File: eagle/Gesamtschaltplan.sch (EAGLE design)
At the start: 26 parts, among them IC3 7818TV, X1 MKDSN1,5/2-5,08, X2 MKDSN1,5/2-5,08, X3 MKDSN1,5/2-5,08

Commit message: Added 'Gesamtschaltplan'
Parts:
- added 1: SUMMER4, 0liver:SUMMER4
- added C10, C11: 22pF, resistor:C-EUC0603K
- added C12, C14: 100 nF, resistor:C-EUC0603
- added C13, C3: 1µ, rcl:CPOL-EUE5-8.5
- added C15, C16, C9: 100 µF, rcl:CPOL-EUE2.5-7
- added C17, C19, C22, C23, C25, C26: 100nF, rcl:C-EUC0805
- added C18, C20, C21: 1000µ, rcl:CPOL-EUE5-13
- added C24: 1000µ, rcl:CPOL-EUE3.5-8
- added C27: 47000 uF, rcl:CPOL-EUE5-9VAXIAL
- added C28, C29: 100000uF, rcl:CPOL-EUE5-9VAXIAL
- added D10, D11, D12, D13, D5, D6, D7, D8, D9: 1N4004, diode:1N4004
- added D14, D15, D16: 38V, diode:ZENER-DIODEC1702-15
- added D4: (no value), diode:ZENER-DIODESOT23
- added DIS1: EA_DIP, display-lcd:EA_DIP
- added F1, F2: (no value), fuse:GSH15
- added IC4: 7818TV, linear:7805TV
- added IC5: DCDC-WANDLER, 0liver:DCDC-WANDLER
- added JP10, JP11, JP13, JP14, JP15, JP16, JP18, JP6: (no value), pinhead:PINHD-1X2
- added JP12: (no value), pinhead:PINHD-1X5
- added JP7: (no value), pinhead:PINHD-1X16
- added JP8: (no value), pinhead:PINHD-2X3
- added JP9: (no value), pinhead:PINHD-1X4
- added LED1, LED2: (no value), led:LED5MM
- added Q1: BC550C, transistor-npn:BC550C
- added Q10, Q11, Q12, Q13, Q14, Q15, Q16, Q17, Q18, Q19, Q20, Q21, Q8, Q9: AUIRF8409, transistor-power:PMOSFET_NTO220BH
- added Q2, Q3, Q4, Q5, Q6, Q7: IRF1234, transistor-power:PMOSFET_NTO220BH
- added R10, R12, R13, R14: 150, resistor:R-EU_0411/15
- added R11: 10k, pot:TRIM_EU-PT10
- added R15, R6, R8: 560, resistor:R-EU_R1206
- added R16, R7, R9: 3k9, resistor:R-EU_R1206
- added R17: 180R, rcl:R-EU_R1206
- added R18, R29, R30, R49: (no value), pot:TRIM_EU-PT10
- added R19, R23, R24, R25, R26, R27, R31, R32, R33, R34, R35, R36, R37: 10R, rcl:R-EU_R1206
- added R22, R38, R47: 50k, rcl:R-EU_R1206
- added R28, R39, R48: 22k 1W, rcl:R-EU_R1206
- added R3: 33k, resistor:R-EU_R1206
- added R4: 220, resistor:R-EU_R1206
- added R40, R41, R42, R43, R44, R45, R46: 10, rcl:R-EU_R1206
- added R5: 150R, rcl:R-EU_R1206
- added R50, R51, R52, R53, R54, R55, R56, R57, R58, R59: 20R 1W, rcl:R-EU_R1206
- added R60: 5R6 50W, rcl:R-EU_R1206
- added R61: 2k, rcl:R-EU_R1206
- added S1: PVA1F, switch-misc:PVA1F
- added S2, S3, S4: 9450-1, switch-misc:9450-1
- added S5: (no value), switch:255SB
- added TR1, TR2: (no value), trafo:EI38-1
- added U$1, U$6: GLEICHRICHTER, Gleichrichter:GLEICHRICHTER
- added U$3, U$4, U$5: MCP1407MCP1407-DIL08, 0liver:MCP1407MCP1407-DIL08
- added U$7: VOLTMETER, 0liver:VOLTMETER
- added X4, X5, X6: MKDSN1,5/2-5,08, con-phoenix-508:MKDSN1,5/2-5,08
- added X7: 1751251, con-phoenix-350:1751251
- C1, C7: value 100nF -> 1n; device rcl:C-EUC0805 -> rcl:C-EUC0603K
- C2: value 1000µ -> 1n; device rcl:CPOL-EUE5-13 -> rcl:C-EUC0603K
- C4: value 1000µ -> 100 nF; device rcl:CPOL-EUE5-13 -> resistor:C-EUC0603
- C5: value 100nF -> 1µ; device rcl:C-EUC0805 -> rcl:CPOL-EUE5-8.5
- C6: value 100nF -> 100 nF; device rcl:C-EUC0805 -> resistor:C-EUC0603
- C8: value 1000µ -> 100 µF; device rcl:CPOL-EUE5-13 -> rcl:CPOL-EUE2.5-7
- D1, D2: value 1N4004 -> (none); device diode:1N4004 -> diode:ZENER-DIODESOT23
- IC1, IC2: value (none) -> LM350T
- IC3: value 7818TV -> ATMEGA328P; device linear:7805TV -> avr-6:MEGA48/88/168-PU
- JP5: device pinhead:PINHD-1X2 -> pinhead:PINHD-1X4
- R1: value 180 -> 150R
- R2: value (none) -> 1k; device pot:TRIM_EU-PT10 -> resistor:R-EU_R1206
- R20: value 180 -> 180R
- U$2: value GLEICHRICHTER -> ABRACON_ABM3_CRYSTALABM03_HC49; device Gleichrichter:GLEICHRICHTER -> Ava:ABRACON_ABM3_CRYSTALABM03_HC49
- X1: value MKDSN1,5/2-5,08 -> MKDSN1,5/3-5,08; device con-phoenix-508:MKDSN1,5/2-5,08 -> con-phoenix-508:MKDSN1,5/3-5,08
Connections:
- removed net N$17: C1.1, C2.+, C4.+, C5.1, C7.1, C8.+, D1.C, D2.C, D3.C, IC1.IN, IC2.IN, IC3.VI, U$2.+
- new net C1V: D7.A, D9.A, JP1.1, JP5.3, R50.1, R51.1, R52.1, R53.1, R54.1, R9.1, U$7.P$1
- new net C1V1: R55.1, R56.1, R57.1, R58.1, R59.1
- new net C2V: C27.+, D12.A, D15.C, D8.C, JP5.1, Q2.D, Q3.D, Q4.D, Q5.D, Q6.D, Q7.D, R28.2, R7.1
- new net DATA0: DIS1.D4, IC3.PD2(INT0/PCINT18), JP7.11
- new net DATA1: DIS1.D5, IC3.PD3(INT1/OC2B/PCINT19), JP7.12
- new net DATA2: DIS1.D6, IC3.PD4(T0/XCK/PCINT20), JP7.13
- new net DATA3: DIS1.D7, IC3.PD5(T1/OC0B/PCINT21), JP7.14
- new net FET1: JP12.5, U$5.IN
- new net FET2: IC3.PD6(AIN0/OC0A/PCINT22), JP12.4, JP9.2, U$4.IN
- new net FET3: IC3.PD7(AIN1/PCINT23), JP12.3, JP9.3, U$3.IN
- new net GND1: C5.-, C6.2, U$4.GND
- new net LED: IC3.PB0(ICP1/CLKO/PCINT0), R4.1
- new net MISO: IC3.PB4(MISO/PCINT4), JP8.1, JP9.1
- new net MOSI: IC3.PB3(MOSI/OC2A/PCINT3), JP8.4
- new net N$1: JP11.1, LED2.A, R5.1
- new net N$10: IC3.PC0(ADC0/PCINT8), JP2.2, S5.S
- new net N$11: LED1.C
- new net N$12: IC3.PC1(ADC1/PCINT9), JP3.2, S4.S
- new net N$13: 1.-, JP4.2, R49.E
- new net N$14: D13.A, R61.2
- new net N$16: C15.-, C16.-, C8.-, C9.-, R10.2, R12.2, R13.2, R14.2
- new net N$18: C2.2, D2.A, IC3.PC2(ADC2/PCINT10), R15.1, R16.2
- new net N$19: S3.S
- new net N$20: IC1.ADJ, JP13.1, R20.1, R29.A
- new net N$21: D8.A
- new net N$22: JP4.1, Q1.E, R49.A, R49.S
- new net N$23: JP14.2, R18.A, R30.E, R30.S
- new net N$26: IC3.PB1(OC1A/PCINT1), R1.2
- new net N$27: C11.1, IC3.PB7(XTAL2/TOSC2/PCINT7), U$2.2
- new net N$35: D12.C, S2.O
- new net N$36: C17.1, C18.+, C19.1, C20.+, C21.+, C22.1, D3.C, D5.C, D6.C, IC1.IN, IC2.IN, IC4.VI, U$1.+
- new net N$37: C23.1, D6.A, IC4.VO, JP16.1
- new net N$38: C24.+, C25.1, IC5.VI, U$6.+
- new net N$39: S12.S, TR1.P1, TR2.P2, X5-1.KL
- new net N$40: F2.2, TR1.P2, X5-2.KL
- new net N$41: TR1.S3, U$6.AC2
- new net N$42: TR1.S4, U$6.AC1
- new net N$43: Q5.G, R19.2
- new net N$44: Q2.G, R23.2
- new net N$45: Q3.G, R24.2
- new net N$46: S12.P, X7-2.K
- new net N$47: DIS1.A, JP7.15, R4.2
- new net N$48: TR2.S4
- new net N$49: S11.P, X7-3.K
- new net N$50: F1.1, F2.1, S11.S
- new net N$51: F1.2, TR2.P1
- new net N$52: Q4.G, R25.2
- new net N$53: Q6.G, R26.2
- new net N$54: Q7.G, R27.2
- new net N$55: R19.1, R22.1, R23.1, R24.1, R25.1, R26.1, R27.1, U$5.OUT, X1-1.KL
- new net N$56: R55.2, R56.2, R57.2, R58.2, R59.2
- new net N$57: D3.A, IC1.OUT, R20.2, R50.2, R51.2, R52.2, R53.2, R54.2, X3-2.KL
- new net N$59: IC2.ADJ, JP14.1, R17.1
- new net N$6: JP6.1, LED1.A, R1.1
- new net N$60: D5.A, IC2.OUT, R17.2, X4-2.KL
- new net N$61: Q8.G, R31.2
- new net N$62: Q9.G, R32.2
- new net N$63: Q10.G, R33.2
- new net N$64: Q11.G, R34.2
- new net N$65: Q12.G, R35.2
- new net N$66: Q13.G, R36.2
- new net N$67: Q14.G, R37.2
- new net N$68: R31.1, R32.1, R33.1, R34.1, R35.1, R36.1, R37.1, R38.1, U$4.OUT, X1-2.KL
- new net N$69: C29.+, D10.A, D14.C, D9.C, Q10.D, Q11.D, Q12.D, Q13.D, Q14.D, Q8.D, Q9.D, R39.2
- new net N$7: C1.2, D1.A, IC3.PC3(ADC3/PCINT11), R6.1, R7.2
- new net N$70: Q15.G, R40.2
- new net N$71: Q16.G, R41.2
- new net N$72: Q17.G, R42.2
- new net N$73: Q18.G, R43.2
- new net N$74: Q19.G, R44.2
- new net N$75: Q20.G, R45.2
- new net N$76: Q21.G, R46.2
- new net N$77: R40.1, R41.1, R42.1, R43.1, R44.1, R45.1, R46.1, R47.1, U$3.OUT, X1-3.KL
- new net N$78: C28.+, D11.A, D16.C, D7.C, Q15.D, Q16.D, Q17.D, Q18.D, Q19.D, Q20.D, Q21.D, R48.2
- new net N$8: DIS1.VEE, JP7.3, R11.S
- new net N$9: IC3.PB2(SS/OC1B/PCINT2), R2.1, R3.1
- new net PE: X7-1.K
- new net RES: IC3.PC6(/RESET/PCINT14), JP8.5
- new net RS: DIS1.RS, IC3.PD0(RXD/PCINT16), JP7.4
- new net RW: DIS1.E, IC3.PD1(TXD/PCINT17), JP7.6
- new net SCK: IC3.PB5(SCK/PCINT5), JP8.3
- new net SENV: D13.C, JP5.4, Q10.S, Q11.S, Q12.S, Q13.S, Q14.S, Q15.S, Q16.S, Q17.S, Q18.S, Q19.S, Q2.S, Q20.S, Q21.S, Q3.S, Q4.S, Q5.S, Q6.S, Q7.S, Q8.S, Q9.S, R16.1, X6-2.KL
- new net VCC: C12.1, C26.1, DIS1.VDD, IC3.AREF, IC3.AVCC, IC3.VCC@1, IC5.VO, JP10.2, JP18.1, JP7.2, JP8.2, Q1.C, R11.A
- net GND: now also 1.+, C1.1, C10.2, C11.2, C12.2, C13.-, C14.2, C17.2, C18.-, C19.2, C2.1, C20.-, C21.-, C22.2, C23.2, C24.-, C25.2, C26.2, C27.-, C28.-, C29.-, C3.-, C4.2, C7.1, D1.C, D14.A, D15.A, D16.A, D2.C, D4.C, DIS1.C, DIS1.R/W, DIS1.VSS, IC3.AGND, IC3.GND@1, IC4.GND, IC5.GND, JP1.2, JP10.1, JP11.2, JP12.1, JP15.1, JP15.2, JP16.2, JP18.2, JP2.1, JP6.2, JP7.1, JP7.16, JP7.5, JP8.6, JP9.4, LED2.C, R10.1, R11.E, R12.1, R13.1, R14.1, R15.2, R18.E, R18.S, R22.2, R28.1, R3.2, R38.2, R39.1, R47.2, R48.1, R6.2, R60.2, R8.2, S5.P, U$1.-, U$3.GND, U$5.GND, U$6.-, U$7.P$2, X4-1.KL, X6-1.KL; no longer C1.2, C2.-, C4.-, C5.2, C6.2, C7.2, C8.-, IC3.GND, JP3.2, JP4.2, R2.E, R2.S, U$2.-, X2-1.KL
- net N$2: now also IC3.PC5(ADC5/SCLPCINT13), R5.2; no longer C6.1, D2.A, IC3.VO, JP4.1, JP5.1
- net N$24: now also U$1.AC1, X2-2.KL; no longer U$2.AC1, X1-2.KL
- net N$25: now also TR2.S3, U$1.AC2, X2-1.KL; no longer U$2.AC2, X1-1.KL
- net N$28: now also C10.1, IC3.PB6(XTAL1/TOSC1/PCINT6), U$2.1; no longer D3.A, IC1.OUT, R20.2, X2-2.KL
- net N$29: now also JP13.2, R29.E, R29.S; no longer JP1.2
- net N$3: now also C13.+, C14.1, C15.+, C16.+, C3.+, C4.1, C5.+, C6.1, C8.+, C9.+, JP12.2, R61.1, U$3.VDD, U$4.VDD, U$5.VDD; no longer D1.A, IC2.OUT, R1.2, X3-2.KL
- net N$30: now also R60.1, S2.P, S3.P; no longer IC1.ADJ, JP1.1, R20.1
- net N$4: now also Q1.B, R2.2; no longer IC2.ADJ, JP2.1, R1.1
- net N$5: now also C7.2, D4.A, IC3.PC4(ADC4/SDA/PCINT12), R8.1, R9.2; no longer JP2.2, R2.A
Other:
- note added: "+18V DC"
- note added: "24V, 3A"
- note added: "5V Vcc"
- note added: "9V, 355mA"
- note added: "Con: Kondensator Supply"
- note added: "Controller"
- note added: "FET Treiber"
- note added: "FET1"
- note added: "Fußtaster"
- note added: "LCD Display"
- note added: "LED"
- note added: "LED2"
- note added: "MCP1407"
- note added: "Mosfet-Treiber"
- note added: "Netzanschluss"
- note added: "Schalter"
- note added: "Schweißelektroden"
- note added: "Spannungs- versorgungsmodul"
- note added: "Spannungversorgung Microcontroller"
- note added: "Voltmeter"
- note added: "Voltmeter 0-35V"
- note added: "Volume"
- moved on the sheet: C1, C6, C7, C8, D3, IC1, IC2, JP1, JP2, JP3, JP4, R1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

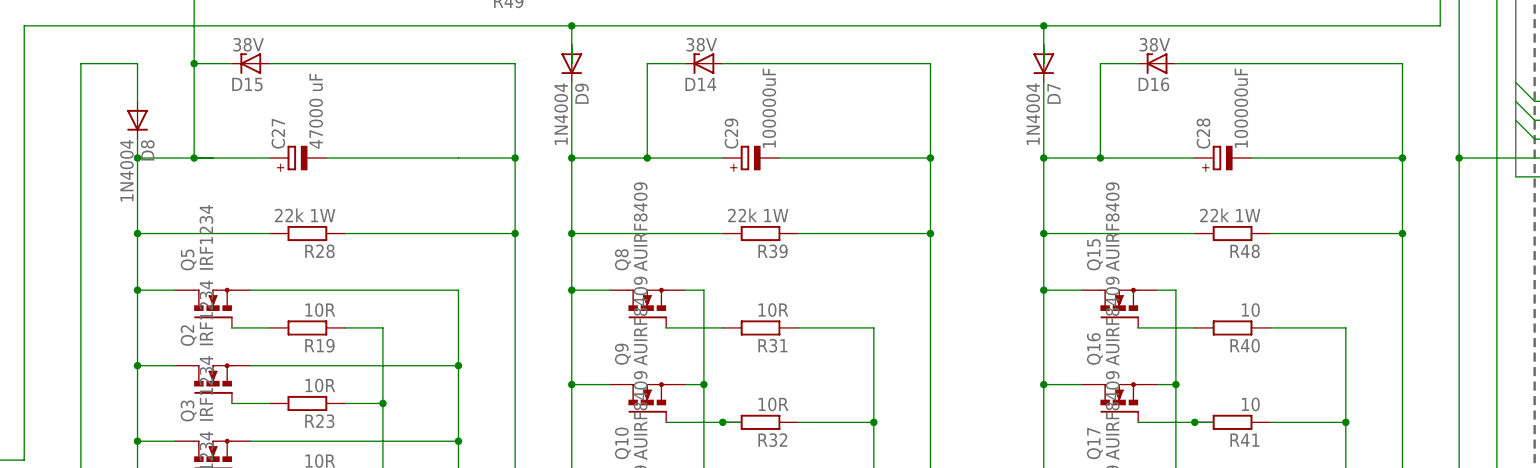
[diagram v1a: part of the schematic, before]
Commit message: Removed 22k Resistor
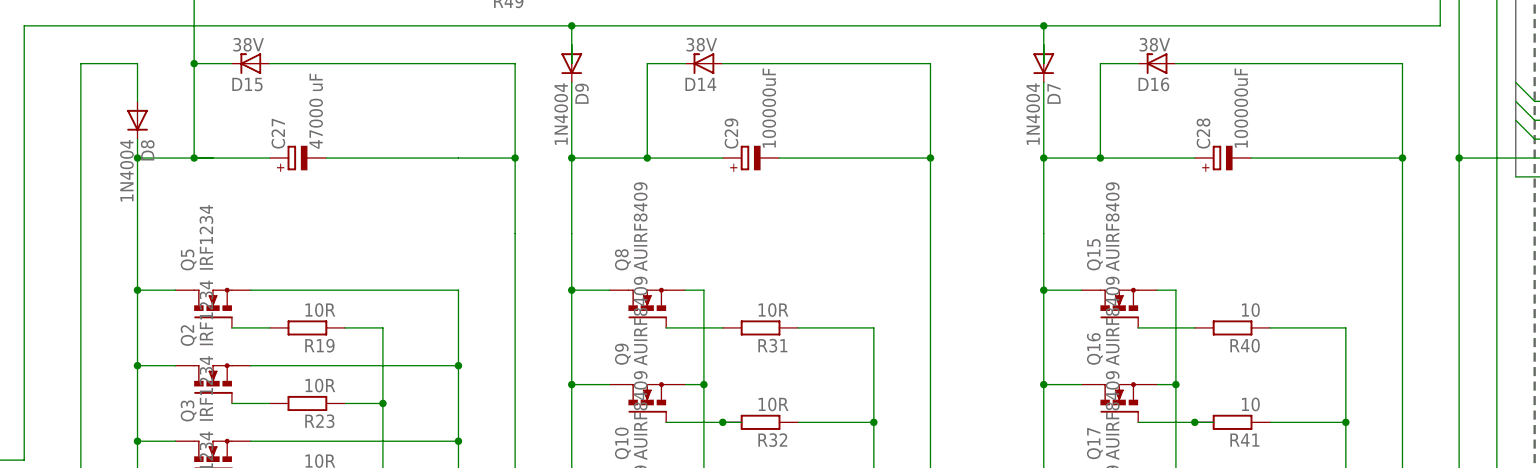
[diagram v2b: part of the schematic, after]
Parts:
- removed R28, R39, R48: 22k 1W, rcl:R-EU_R1206
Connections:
- net C2V: no longer R28.2
- net GND: no longer R28.1, R39.1, R48.1
- net N$69: no longer R39.2
- net N$78: no longer R48.2
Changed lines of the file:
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@@
 <part name="R22" library="rcl" deviceset="R-EU_" device="R1206" value="50k"/>
 <part name="GND52" library="supply1" deviceset="GND" device=""/>
-<part name="R28" library="rcl" deviceset="R-EU_" device="R1206" value="22k 1W"/>
 <part name="R29" library="pot" deviceset="TRIM_EU-" device="PT10"/>
 <part name="R30" library="pot" deviceset="TRIM_EU-" device="PT10"/>
@@
 <part name="R37" library="rcl" deviceset="R-EU_" device="R1206" value="10R"/>
 <part name="R38" library="rcl" deviceset="R-EU_" device="R1206" value="50k"/>
-<part name="R39" library="rcl" deviceset="R-EU_" device="R1206" value="22k 1W"/>
 <part name="C27" library="rcl" deviceset="CPOL-EU" device="E5-9VAXIAL" value="47000 uF"/>
 <part name="C29" library="rcl" deviceset="CPOL-EU" device="E5-9VAXIAL" value="100000uF"/>
@@
 <part name="R46" library="rcl" deviceset="R-EU_" device="R1206" value="10"/>
 <part name="R47" library="rcl" deviceset="R-EU_" device="R1206" value="50k"/>
-<part name="R48" library="rcl" deviceset="R-EU_" device="R1206" value="22k 1W"/>
 <part name="C28" library="rcl" deviceset="CPOL-EU" device="E5-9VAXIAL" value="100000uF"/>
 <part name="D7" library="diode" deviceset="1N4004" device=""/>
@@
 <instance part="R22" gate="G$1" x="76.2" y="-165.1" rot="R270"/>
 <instance part="GND52" gate="1" x="76.2" y="-175.26"/>
-<instance part="R28" gate="G$1" x="66.04" y="-91.44" rot="R180"/>
 <instance part="R29" gate="1" x="30.48" y="-154.94" rot="R180"/>
 <instance part="R30" gate="1" x="30.48" y="-233.68" rot="R180"/>
@@
 <instance part="R37" gate="G$1" x="127" y="-180.34" rot="R180"/>
 <instance part="R38" gate="G$1" x="142.24" y="-190.5" rot="R270"/>
-<instance part="R39" gate="G$1" x="127" y="-91.44" rot="R180"/>
 <instance part="C27" gate="G$1" x="63.5" y="-81.28" rot="R90"/>
 <instance part="C29" gate="G$1" x="124.46" y="-81.28" rot="R90"/>
@@
 <instance part="R46" gate="G$1" x="190.5" y="-180.34" rot="R180"/>
 <instance part="R47" gate="G$1" x="205.74" y="-190.5" rot="R270"/>
-<instance part="R48" gate="G$1" x="190.5" y="-91.44" rot="R180"/>
 <instance part="C28" gate="G$1" x="187.96" y="-81.28" rot="R90"/>
 <instance part="D7" gate="1" x="165.1" y="-68.58" rot="R270"/>
@@
 <wire x1="149.86" y1="-81.28" x2="149.86" y2="-91.44" width="0.1524" layer="91"/>
 <wire x1="149.86" y1="-91.44" x2="149.86" y2="-203.2" width="0.1524" layer="91"/>
-<junction x="149.86" y="-91.44"/>
-<pinref part="R39" gate="G$1" pin="1"/>
-<wire x1="132.08" y1="-91.44" x2="149.86" y2="-91.44" width="0.1524" layer="91"/>
 <pinref part="C28" gate="G$1" pin="-"/>
 <wire x1="193.04" y1="-81.28" x2="213.36" y2="-81.28" width="0.1524" layer="91"/>
@@
 <wire x1="213.36" y1="-91.44" x2="213.36" y2="-208.28" width="0.1524" layer="91"/>
 <wire x1="213.36" y1="-208.28" x2="157.48" y2="-208.28" width="0.1524" layer="91"/>
-<pinref part="R48" gate="G$1" pin="1"/>
-<wire x1="195.58" y1="-91.44" x2="213.36" y2="-91.44" width="0.1524" layer="91"/>
-<junction x="213.36" y="-91.44"/>
 <wire x1="93.98" y1="-226.06" x2="93.98" y2="-208.28" width="0.1524" layer="91"/>
 <wire x1="93.98" y1="-208.28" x2="93.98" y2="-203.2" width="0.1524" layer="91"/>
@@
 <wire x1="68.58" y1="-81.28" x2="86.36" y2="-81.28" width="0.1524" layer="91"/>
 <wire x1="86.36" y1="-81.28" x2="93.98" y2="-81.28" width="0.1524" layer="91"/>
-<pinref part="R28" gate="G$1" pin="1"/>
-<wire x1="71.12" y1="-91.44" x2="93.98" y2="-91.44" width="0.1524" layer="91"/>
-<junction x="93.98" y="-91.44"/>
 <pinref part="C27" gate="G$1" pin="-"/>
 <wire x1="157.48" y1="-208.28" x2="149.86" y2="-208.28" width="0.1524" layer="91"/>
@@
 <junction x="43.18" y="-99.06"/>
 <wire x1="43.18" y1="-99.06" x2="43.18" y2="-91.44" width="0.1524" layer="91"/>
-<pinref part="R28" gate="G$1" pin="2"/>
-<wire x1="60.96" y1="-91.44" x2="43.18" y2="-91.44" width="0.1524" layer="91"/>
-<junction x="43.18" y="-91.44"/>
 <wire x1="43.18" y1="-91.44" x2="43.18" y2="-88.9" width="0.1524" layer="91"/>
 <wire x1="43.18" y1="-81.28" x2="43.18" y2="-88.9" width="0.1524" layer="91"/>
@@
 <wire x1="101.6" y1="-91.44" x2="101.6" y2="-81.28" width="0.1524" layer="91"/>
 <wire x1="101.6" y1="-81.28" x2="111.76" y2="-81.28" width="0.1524" layer="91"/>
-<pinref part="R39" gate="G$1" pin="2"/>
 <wire x1="111.76" y1="-81.28" x2="121.92" y2="-81.28" width="0.1524" layer="91"/>
-<wire x1="121.92" y1="-91.44" x2="101.6" y2="-91.44" width="0.1524" layer="91"/>
-<junction x="101.6" y="-91.44"/>
 <wire x1="101.6" y1="-71.12" x2="101.6" y2="-81.28" width="0.1524" layer="91"/>
 <junction x="101.6" y="-81.28"/>
@@
 <wire x1="165.1" y1="-91.44" x2="165.1" y2="-81.28" width="0.1524" layer="91"/>
 <wire x1="165.1" y1="-81.28" x2="172.72" y2="-81.28" width="0.1524" layer="91"/>
-<pinref part="R48" gate="G$1" pin="2"/>
 <wire x1="172.72" y1="-81.28" x2="185.42" y2="-81.28" width="0.1524" layer="91"/>
-<wire x1="185.42" y1="-91.44" x2="165.1" y2="-91.44" width="0.1524" layer="91"/>
-<junction x="165.1" y="-91.44"/>
 <wire x1="165.1" y1="-71.12" x2="165.1" y2="-81.28" width="0.1524" layer="91"/>
 <junction x="165.1" y="-81.28"/>

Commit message: Corrected wrong direction of zener diodes
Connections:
- net GND: now also D1.A, D2.A, D4.A; no longer D1.C, D2.C, D4.C
- net N$18: now also D2.C; no longer D2.A
- net N$5: now also D4.C; no longer D4.A
- net N$7: now also D1.C; no longer D1.A
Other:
- moved on the sheet: D1, D2, D4
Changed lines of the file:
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@@
 <instance part="JP3" gate="G$1" x="55.88" y="96.52" rot="R90"/>
 <instance part="GND8" gate="1" x="53.34" y="81.28"/>
-<instance part="D4" gate="G$1" x="93.98" y="93.98" rot="R90"/>
+<instance part="D4" gate="G$1" x="93.98" y="93.98" rot="R270"/>
 <instance part="R8" gate="G$1" x="101.6" y="93.98" rot="R90"/>
 <instance part="C7" gate="G$1" x="109.22" y="96.52"/>
@@
 <instance part="GND1" gate="1" x="193.04" y="10.16"/>
 <instance part="JP11" gate="G$1" x="205.74" y="17.78"/>
-<instance part="D1" gate="G$1" x="129.54" y="93.98" rot="R90"/>
+<instance part="D1" gate="G$1" x="129.54" y="93.98" rot="R270"/>
 <instance part="R6" gate="G$1" x="137.16" y="93.98" rot="R90"/>
 <instance part="C1" gate="G$1" x="144.78" y="96.52"/>
 <instance part="R7" gate="G$1" x="144.78" y="76.2" rot="R90"/>
 <instance part="GND4" gate="1" x="152.4" y="91.44"/>
-<instance part="D2" gate="G$1" x="165.1" y="93.98" rot="R90"/>
+<instance part="D2" gate="G$1" x="165.1" y="93.98" rot="R270"/>
 <instance part="R15" gate="G$1" x="172.72" y="93.98" rot="R90"/>
 <instance part="C2" gate="G$1" x="180.34" y="96.52"/>
@@
 </segment>
 <segment>
-<pinref part="D4" gate="G$1" pin="C"/>
 <pinref part="R8" gate="G$1" pin="2"/>
 <pinref part="C7" gate="G$1" pin="1"/>
@@
 <junction x="101.6" y="101.6"/>
 <wire x1="101.6" y1="101.6" x2="93.98" y2="101.6" width="0.1524" layer="91"/>
-<wire x1="93.98" y1="101.6" x2="93.98" y2="96.52" width="0.1524" layer="91"/>
 <pinref part="GND9" gate="1" pin="GND"/>
 <wire x1="109.22" y1="101.6" x2="116.84" y2="101.6" width="0.1524" layer="91"/>
 <wire x1="116.84" y1="101.6" x2="116.84" y2="93.98" width="0.1524" layer="91"/>
 <junction x="109.22" y="101.6"/>
-</segment>
-<segment>
-<pinref part="D1" gate="G$1" pin="C"/>
+<pinref part="D4" gate="G$1" pin="A"/>
+<wire x1="93.98" y1="96.52" x2="93.98" y2="101.6" width="0.1524" layer="91"/>
+</segment>
+<segment>
 <pinref part="R6" gate="G$1" pin="2"/>
 <pinref part="C1" gate="G$1" pin="1"/>
@@
 <junction x="137.16" y="101.6"/>
 <wire x1="137.16" y1="101.6" x2="129.54" y2="101.6" width="0.1524" layer="91"/>
-<wire x1="129.54" y1="101.6" x2="129.54" y2="96.52" width="0.1524" layer="91"/>
 <pinref part="GND4" gate="1" pin="GND"/>
 <wire x1="144.78" y1="101.6" x2="152.4" y2="101.6" width="0.1524" layer="91"/>
 <wire x1="152.4" y1="101.6" x2="152.4" y2="93.98" width="0.1524" layer="91"/>
 <junction x="144.78" y="101.6"/>
-</segment>
-<segment>
-<pinref part="D2" gate="G$1" pin="C"/>
+<pinref part="D1" gate="G$1" pin="A"/>
+<wire x1="129.54" y1="96.52" x2="129.54" y2="101.6" width="0.1524" layer="91"/>
+</segment>
+<segment>
 <pinref part="R15" gate="G$1" pin="2"/>
 <pinref part="C2" gate="G$1" pin="1"/>
@@
 <junction x="172.72" y="101.6"/>
 <wire x1="172.72" y1="101.6" x2="165.1" y2="101.6" width="0.1524" layer="91"/>
-<wire x1="165.1" y1="101.6" x2="165.1" y2="96.52" width="0.1524" layer="91"/>
 <pinref part="GND5" gate="1" pin="GND"/>
 <wire x1="180.34" y1="101.6" x2="187.96" y2="101.6" width="0.1524" layer="91"/>
 <wire x1="187.96" y1="101.6" x2="187.96" y2="93.98" width="0.1524" layer="91"/>
 <junction x="180.34" y="101.6"/>
+<pinref part="D2" gate="G$1" pin="A"/>
+<wire x1="165.1" y1="96.52" x2="165.1" y2="101.6" width="0.1524" layer="91"/>
 </segment>
 <segment>
@@
 <wire x1="83.82" y1="68.58" x2="83.82" y2="106.68" width="0.1524" layer="91"/>
 <wire x1="83.82" y1="106.68" x2="160.02" y2="106.68" width="0.1524" layer="91"/>
-<pinref part="D2" gate="G$1" pin="A"/>
-<wire x1="165.1" y1="86.36" x2="165.1" y2="91.44" width="0.1524" layer="91"/>
 <wire x1="180.34" y1="83.82" x2="172.72" y2="83.82" width="0.1524" layer="91"/>
 <wire x1="172.72" y1="83.82" x2="165.1" y2="83.82" width="0.1524" layer="91"/>
@@
 <junction x="180.34" y="83.82"/>
 <wire x1="160.02" y1="106.68" x2="160.02" y2="83.82" width="0.1524" layer="91"/>
+<pinref part="D2" gate="G$1" pin="C"/>
+<wire x1="165.1" y1="86.36" x2="165.1" y2="91.44" width="0.1524" layer="91"/>
 </segment>
 </net>
@@
 <net name="N$5" class="0">
 <segment>
-<pinref part="D4" gate="G$1" pin="A"/>
-<wire x1="93.98" y1="86.36" x2="93.98" y2="91.44" width="0.1524" layer="91"/>
 <wire x1="109.22" y1="83.82" x2="101.6" y2="83.82" width="0.1524" layer="91"/>
 <wire x1="101.6" y1="83.82" x2="93.98" y2="83.82" width="0.1524" layer="91"/>
-<wire x1="93.98" y1="86.36" x2="93.98" y2="83.82" width="0.1524" layer="91"/>
 <pinref part="R8" gate="G$1" pin="1"/>
 <wire x1="101.6" y1="88.9" x2="101.6" y2="83.82" width="0.1524" layer="91"/>
@@
 <wire x1="93.98" y1="83.82" x2="88.9" y2="83.82" width="0.1524" layer="91"/>
 <wire x1="88.9" y1="83.82" x2="88.9" y2="63.5" width="0.1524" layer="91"/>
-<junction x="93.98" y="83.82"/>
 <wire x1="109.22" y1="81.28" x2="109.22" y2="83.82" width="0.1524" layer="91"/>
 <junction x="109.22" y="83.82"/>
+<pinref part="D4" gate="G$1" pin="C"/>
+<wire x1="93.98" y1="83.82" x2="93.98" y2="91.44" width="0.1524" layer="91"/>
+<junction x="93.98" y="83.82"/>
 </segment>
 </net>
 <net name="N$7" class="0">
 <segment>
-<pinref part="D1" gate="G$1" pin="A"/>
-<wire x1="129.54" y1="86.36" x2="129.54" y2="91.44" width="0.1524" layer="91"/>
 <wire x1="144.78" y1="83.82" x2="137.16" y2="83.82" width="0.1524" layer="91"/>
 <wire x1="137.16" y1="83.82" x2="129.54" y2="83.82" width="0.1524" layer="91"/>
@@
 <wire x1="86.36" y1="66.04" x2="86.36" y2="104.14" width="0.1524" layer="91"/>
 <wire x1="124.46" y1="104.14" x2="86.36" y2="104.14" width="0.1524" layer="91"/>
-</segment>
-</net>
+<pinref part="D1" gate="G$1" pin="C"/>
+<wire x1="129.54" y1="86.36" x2="129.54" y2="91.44" width="0.1524" layer="91"/>
+</segment>
+</net>
